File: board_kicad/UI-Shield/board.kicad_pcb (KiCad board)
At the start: 2 copper layers, 101.6 x 53.3 mm, 34 parts, among them Q1 Q_NPN_BEC, SW1 1, SW2 SW_Push, SW3 SW_Push, SW4 SW_Push, SW5 SW_Push_LED, SW6 SW_Push_LED, SW7 SW_Push_LED, SW8 SW_Push_LED, U1 MCP23S17_SS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

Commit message: added values and manufacurer id (kicost), improvements
BOTH
- added missing values for resitors and diodes
- added manf# for calculating and ordering with kicost
- minor improvements

NanoE-dmx
- bus controll LEDs (buffered) fixed for TX/RX, SDA/SCL
- changed J40 (RJ45(8pol)->Conn(4pol)
- added ISO 5V LED

UI-Shield
- Replaced U2 (MAX5026->LM2705), for higher max current
- added 2 leds at NC IO ports
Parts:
- added D2: LED, LED_SMD:LED_0805_2012Metric, F.Cu at (177.2, 92.1)
- added D3: LED, LED_SMD:LED_0805_2012Metric, F.Cu at (177.2, 96.5)
- added R10: 560, Resistor_SMD:R_0805_2012Metric, F.Cu at (167.6, 78.1)
- added R11: 560, Resistor_SMD:R_0805_2012Metric, F.Cu at (162.9, 78.1)
- JP1: value SolderJumper_2_Bridged -> SolderJumper_2_Open; footprint Jumper:SolderJumper-2_P1.3mm_Bridged2Bar_Pad1.0x1.5mm -> Jumper:SolderJumper-2_P1.3mm_Open_Pad1.0x1.5mm
- L1: value 47uH -> 33uH
- Q1: value Q_NPN_BEC -> BSR14
- R2: value R -> 240k
- R3: value R -> 27k
- R4: value R -> 910k
- R5, R6, R7, R8: value R -> 150
- R9: value R -> 20
- U2: value MAX5026 -> LM2705; footprint Package_TO_SOT_SMD:SOT-23-6 -> Package_TO_SOT_SMD:SOT-23-5
- XA1: value Arduino_Uno_Shield -> Arduino_Shield
- moved R2 8.52 mm to (148.6, 106.0)
- moved C5 7.94 mm to (150.5, 102.2), turned to 90 degrees
- moved C4 7.54 mm to (156.8, 103.2)
- moved R3 5.72 mm to (150.5, 106.0), turned to 90 degrees
- moved L1 3.91 mm to (155.8, 99.4)
- moved C6 2.26 mm to (153.7, 95.6)
- moved U2 2.01 mm to (153.7, 104.1), turned to 0 degrees
- moved R1 1.91 mm to (150.7, 96.5)
- moved D1 0.55 mm to (151.8, 99.4), turned to 0 degrees
- moved JP1 0.13 mm to (152.9, 80.0)
- turned C1 to 90 degrees
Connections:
- C1 pad 1: Net-(C1-Pad1) -> +5V
- C1 pad 2: +5V -> Net-(C1-Pad2)
- LCD2 pad 4: Net-(C1-Pad1) -> Net-(C1-Pad2)
- U1 pad 27: Net-(U1-Pad27) -> /LED1
- U1 pad 28: Net-(U1-Pad28) -> /LED2
- U2 pad 1: GND -> Net-(D1-Pad2)
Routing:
- net Net-(D3-Pad2): track 0.00 -> 29.8 mm
- net Net-(D2-Pad2): track 0.00 -> 17.4 mm
- net Net-(C1-Pad2): track 0.00 -> 15.4 mm
- net Net-(C1-Pad1): track 15.4 -> 0.00 mm
- net /LED1: track 0.00 -> 11.2 mm
- net GND: track 104.6 -> 94.9 mm, vias 8 -> 10
- net +5V: track 24.5 -> 16.7 mm
- net /LED2: track 0.00 -> 6.02 mm
- net +12V: track 78.6 -> 75.4 mm
- net Net-(C5-Pad2): track 11.3 -> 8.52 mm
- net /LCD_LED: track 89.1 -> 89.9 mm
- net Net-(D1-Pad2): track 5.09 -> 5.70 mm
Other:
- board text added: "INTA"
- board text added: "INTA-D2"
- board text added: "INTB"
- board text added: "INTB-D3"
- board text added: "LED1"
- board text added: "LED2"

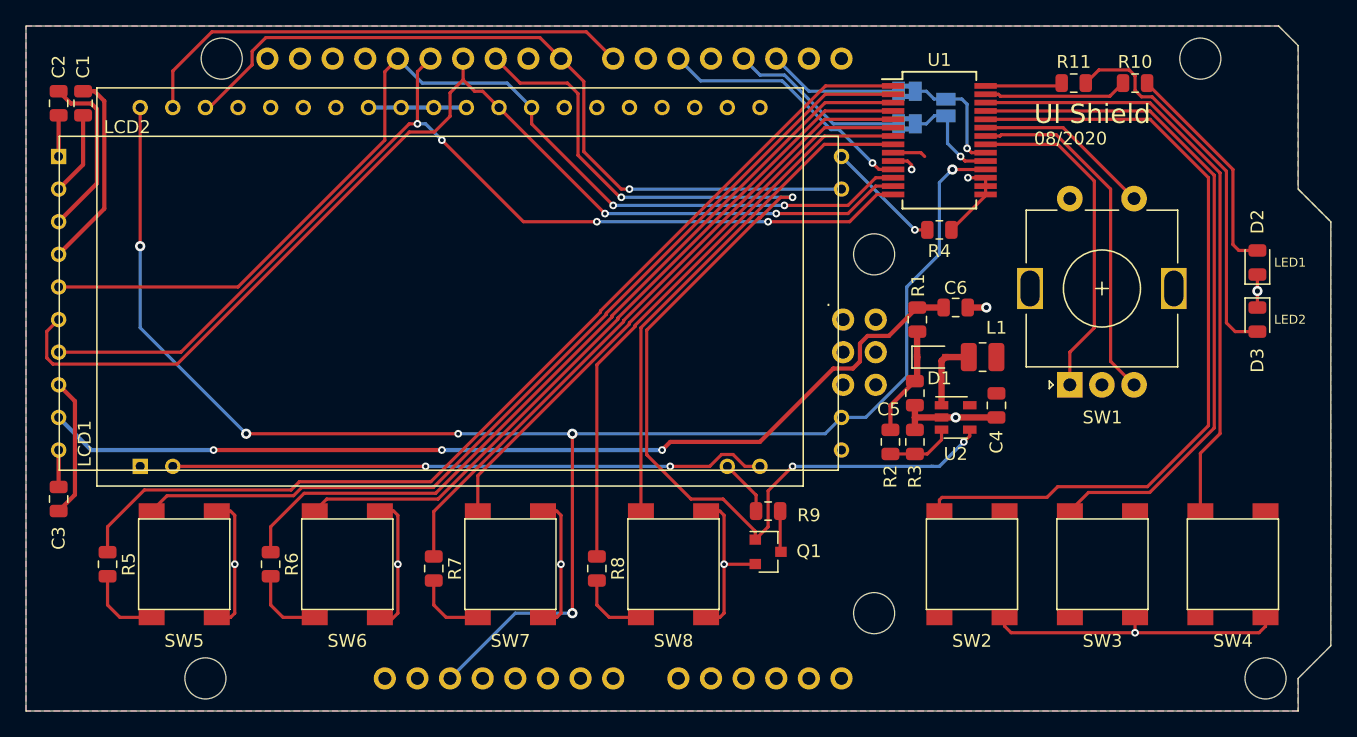
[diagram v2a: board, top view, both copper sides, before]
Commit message: fixed errors in NanoE-DMX and UI-Shield
NanoE-DMX -> Rev: 1.0:
- see previous commit
- fixed footprint of U1
- reroutet corresponding tracks
- added ICSP header to board

UI-Shield -> Rev: 1.0:
- added ICSP header to board
- optional (exclusive) I2C for OLED and IO-Expander
- selectable SPI source (ICSP/D12-D10)
- fixed LCD SPI interchanged communication lines
- added dimming for LED-Buttons and LEDs
- fixed erros in OLED routing
	- I2C only tested on plugboard
	- SPI not testet
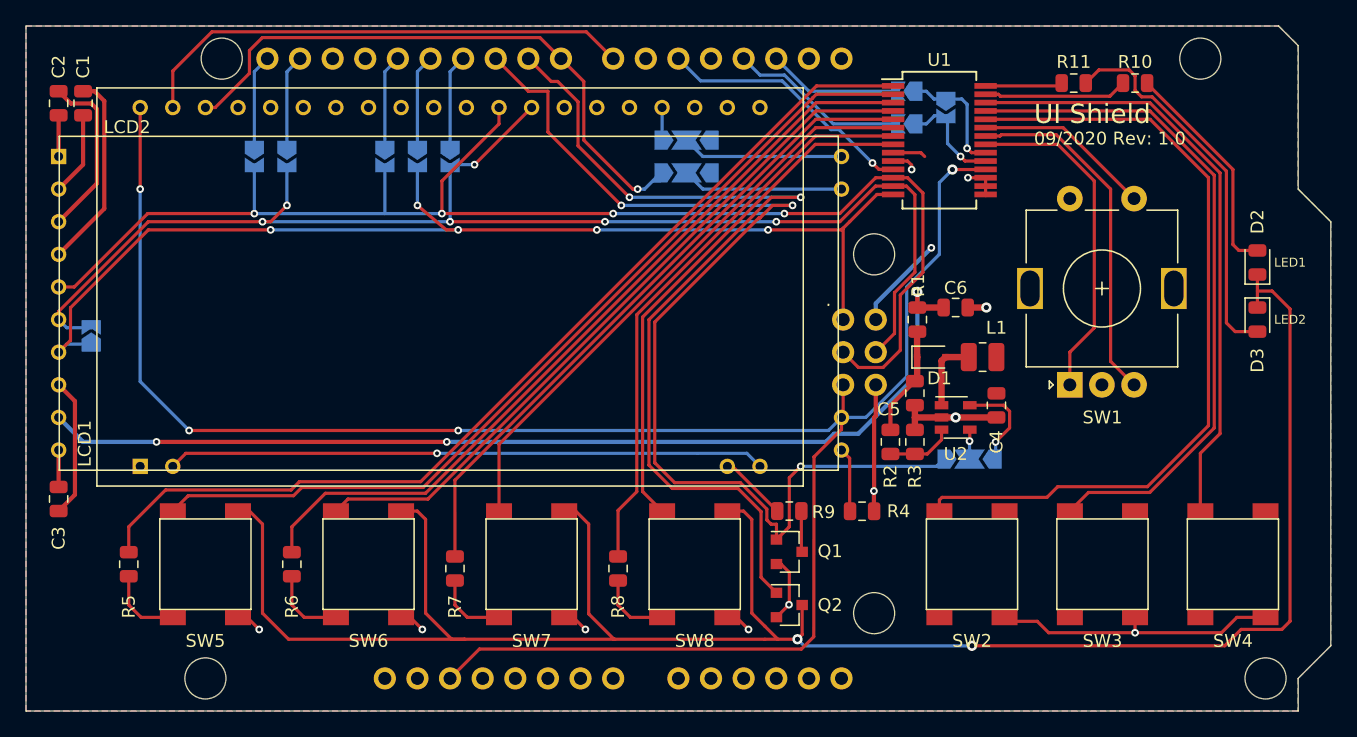
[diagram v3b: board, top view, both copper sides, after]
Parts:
- added JP10: SolderJumper_3_Open, Jumper:SolderJumper-3_P2.0mm_Open_TrianglePad1.0x1.5mm, B.Cu at (154.7, 107.4)
- added JP11: SolderJumper_3_Open, Jumper:SolderJumper-3_P2.0mm_Open_TrianglePad1.0x1.5mm, B.Cu at (132.7, 85.1)
- added JP12: SolderJumper_3_Open, Jumper:SolderJumper-3_P2.0mm_Open_TrianglePad1.0x1.5mm, B.Cu at (132.7, 82.5)
- added JP4: SolderJumper_2_Open, Jumper:SolderJumper-2_P1.3mm_Open_TrianglePad1.0x1.5mm, B.Cu at (114.3, 83.8)
- added JP5: SolderJumper_2_Open, Jumper:SolderJumper-2_P1.3mm_Open_TrianglePad1.0x1.5mm, B.Cu at (111.8, 83.8)
- added JP6: SolderJumper_2_Open, Jumper:SolderJumper-2_P1.3mm_Open_TrianglePad1.0x1.5mm, B.Cu at (109.2, 83.8)
- added JP7: SolderJumper_2_Open, Jumper:SolderJumper-2_P1.3mm_Open_TrianglePad1.0x1.5mm, B.Cu at (86.4, 97.8)
- added JP8: SolderJumper_2_Open, Jumper:SolderJumper-2_P1.3mm_Open_TrianglePad1.0x1.5mm, B.Cu at (101.6, 83.8)
- added JP9: SolderJumper_2_Open, Jumper:SolderJumper-2_P1.3mm_Open_TrianglePad1.0x1.5mm, B.Cu at (99.1, 83.8)
- added Q2: BSR14, Package_TO_SOT_SMD:SOT-23, F.Cu at (140.7, 118.7)
- JP1: footprint Jumper:SolderJumper-2_P1.3mm_Open_Pad1.0x1.5mm -> Jumper:SolderJumper-2_P1.3mm_Open_TrianglePad1.0x1.5mm
- JP2, JP3: value SolderJumper_2_Bridged -> SolderJumper_2_Open; footprint Jumper:SolderJumper-2_P1.3mm_Bridged2Bar_Pad1.0x1.5mm -> Jumper:SolderJumper-2_P1.3mm_Open_TrianglePad1.0x1.5mm
- moved R4 22.7 mm to (146.4, 111.4)
- moved Q1 1.65 mm to (140.7, 114.6)
- moved R5 1.65 mm to (89.3, 115.6)
- moved R9 1.65 mm to (140.7, 111.4)
- moved SW7 1.65 mm to (120.7, 115.6)
- moved R6 1.65 mm to (102.0, 115.6)
- moved R7 1.65 mm to (114.7, 115.9)
- moved R8 1.65 mm to (127.4, 115.9)
- moved SW5 1.65 mm to (95.2, 115.6)
- moved SW6 1.65 mm to (108.0, 115.6)
- moved SW8 1.65 mm to (133.3, 115.6)
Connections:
- D2 pad 1: GND -> Net-(D2-Pad1)
- D3 pad 1: GND -> Net-(D2-Pad1)
- LCD1 pad 28: /SCK -> /MOSI
- LCD1 pad 29: /MOSI -> /SCK
- LCD2 pad 11: GND -> Net-(LCD2-Pad11)
- LCD2 pad 19: /LCD_CS -> /_LCD_CS
- LCD2 pad 20: Net-(LCD2-Pad20) -> /BS1
- R4 pad 2: Net-(LCD2-Pad20) -> Net-(LCD2-Pad11)
- SW5 pad 3: GND -> Net-(D2-Pad1)
- SW6 pad 3: GND -> Net-(D2-Pad1)
- SW7 pad 3: GND -> Net-(D2-Pad1)
- SW8 pad 3: GND -> Net-(D2-Pad1)
- U2 pad 4: /LCD_LED -> /12V_EN
- XA1 pad 5V2: Net-(XA1-Pad5V2) -> +5V
- XA1 pad D11: /MOSI -> Net-(JP4-Pad1)
- XA1 pad D12: /MISO -> Net-(JP5-Pad1)
- XA1 pad D13: /SCK -> Net-(JP6-Pad1)
- XA1 pad D9: /D9 -> /SW_LED
- XA1 pad GND4: Net-(XA1-PadGND4) -> GND
- XA1 pad MISO: Net-(XA1-PadMISO) -> /MISO
- XA1 pad MOSI: Net-(XA1-PadMOSI) -> /MOSI
- XA1 pad RST2: Net-(XA1-PadRST2) -> /~RESET
- XA1 pad SCK: Net-(XA1-PadSCK) -> /SCK
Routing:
- net Net-(D2-Pad1): track 0.00 -> 163.0 mm, vias 0 -> 2
- net /SW_LED: track 0.00 -> 71.8 mm, vias 0 -> 2
- net GND: track 94.9 -> 65.9 mm, vias 10 -> 11
- net /~RESET: track 127.9 -> 154.7 mm, vias 6 -> 4
- net /SCK: track 81.8 -> 107.4 mm, vias 2 -> 4
- net /MOSI: track 86.6 -> 106.2 mm, vias 2 -> 6
- net /LCD_CS: track 60.5 -> 47.4 mm
- net /_LCD_CS: track 0.00 -> 12.6 mm
- net /BS1: track 0.00 -> 12.6 mm
- net +5V: track 16.7 -> 26.6 mm, vias 0 -> 2
- net Net-(LCD2-Pad20): track 9.05 -> 0.00 mm, vias 1 -> 0
- net Net-(JP6-Pad1): track 0.00 -> 7.39 mm
- net Net-(JP4-Pad1): track 0.00 -> 7.39 mm
- net /SDA: track 0.00 -> 7.39 mm
- net Net-(JP5-Pad1): track 0.00 -> 7.39 mm
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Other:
- board text added: "+5V-EN_12V-D10"
- board text added: "09/2020 Rev: 1.0"
- board text added: "A SPI"
- board text added: "B SPI"
- board text added: "C I2C"
- board text added: "MOSI-MISO"
- board text added: "OLED I2C SPI"
- board text removed: "08/2020"
